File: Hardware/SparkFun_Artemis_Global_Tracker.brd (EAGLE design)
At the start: 50.8 x 63.5 mm, 209 parts, among them J1 IRIDIUM_9603N, J2 USB-C, J6 U.FL, J7 ANTENNA-GROUNDEDEDGE_SMA, J8 STANDOFFS_M2X0.4_STEEL_6MM, J9 STANDOFFS_M2X0.4_STEEL_6MM, Q1 5.8A/30V/35mΩ, Q2 20V/4.2A/52mΩ/1.4W, Q3 20V/4.2A/52mΩ/1.4W, Q4 600mA/40V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

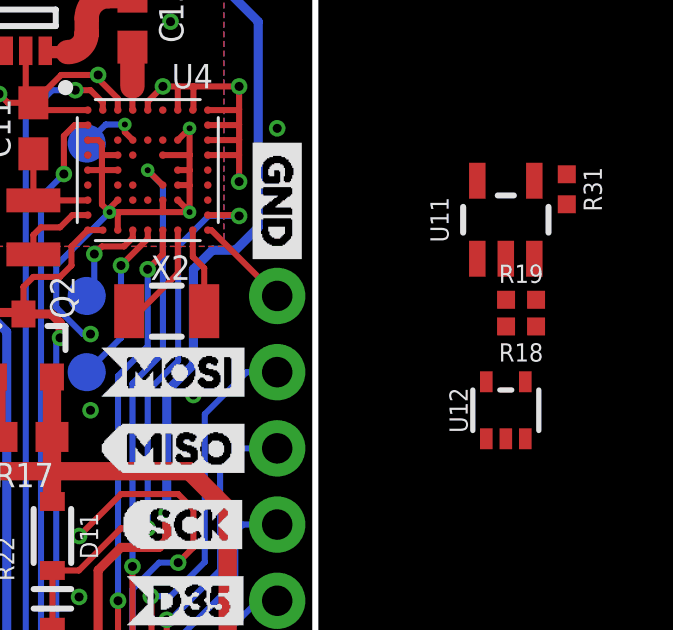
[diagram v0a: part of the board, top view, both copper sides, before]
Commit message: swapping names of U11 and U12 to avoid confusion
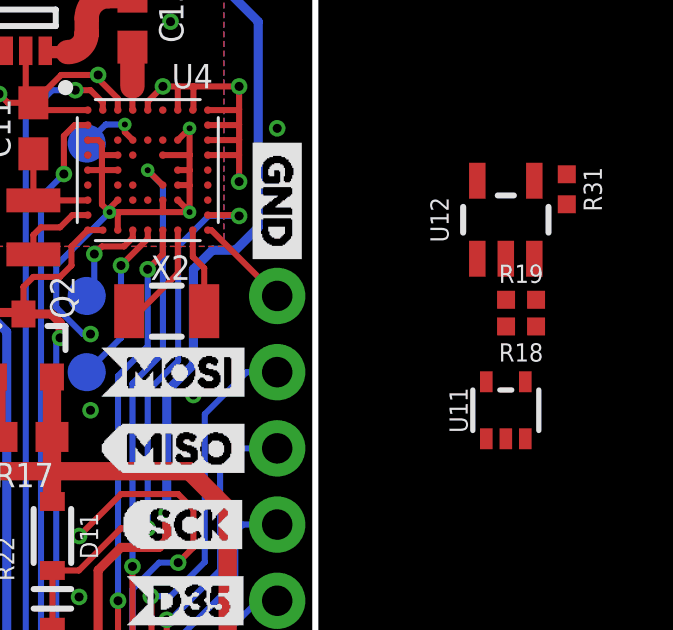
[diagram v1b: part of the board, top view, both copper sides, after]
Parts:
- U11: value 74LVC1G08SE -> 74LVC1G04SE; device SparkFun-IC-Logic:SOT23-5 -> SparkFun-IC-Logic:SOT353
- U12: value 74LVC1G04SE -> 74LVC1G08SE; device SparkFun-IC-Logic:SOT353 -> SparkFun-IC-Logic:SOT23-5
- moved U11 6.35 mm to (57.1, 41.9)
- moved U12 6.35 mm to (57.1, 48.3)
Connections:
- net 3.3V: now also U12.5; no longer U11.5
- net 3V3SW: now also U12.1; no longer U11.1
- net EXT_PWR: now also U11.2; no longer U12.2
- net LTC3225_VOUT: now also U11.5; no longer U12.5
- net N$31: now also U12.4; no longer U11.4
- net N$33: now also U12.2; no longer U11.2
- net N$7: now also U11.4; no longer U12.4
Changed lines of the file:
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@@
 <drawing>
 <settings>
-<setting alwaysvectorfont="yes"/>
+<setting alwaysvectorfont="no"/>
 <setting keepoldvectorfont="yes"/>
 <setting verticaltext="up"/>
@@
 <layer number="47" name="Measures" color="7" fill="1" visible="no" active="yes"/>
 <layer number="48" name="Document" color="7" fill="1" visible="no" active="yes"/>
-<layer number="49" name="Reference" color="7" fill="1" visible="yes" active="yes"/>
+<layer number="49" name="Reference" color="7" fill="1" visible="no" active="yes"/>
 <layer number="50" name="dxf" color="7" fill="1" visible="no" active="yes"/>
 <layer number="51" name="tDocu" color="6" fill="1" visible="yes" active="yes"/>
@@
 <attribute name="VALUE" x="57.658" y="45.031" size="0.6096" layer="27" font="vector" ratio="20" align="top-center"/>
 </element>
-<element name="U11" library="SparkFun-IC-Logic" package="SOT23-5" value="74LVC1G08SE" x="57.15" y="48.26" smashed="yes">
+<element name="U12" library="SparkFun-IC-Logic" package="SOT23-5" value="74LVC1G08SE" x="57.15" y="48.26" smashed="yes">
 <attribute name="NAME" x="55.245" y="48.26" size="0.6096" layer="25" font="vector" ratio="20" rot="R90" align="bottom-center"/>
 <attribute name="PROD_ID" value="IC-10841" x="57.15" y="48.26" size="1.778" layer="27" font="vector" ratio="15" display="off"/>
 <attribute name="VALUE" x="59.69" y="48.26" size="0.6096" layer="27" font="vector" ratio="20" rot="R90" align="bottom-center"/>
 </element>
-<element name="U12" library="SparkFun-IC-Logic" package="SOT353" value="74LVC1G04SE" x="57.15" y="41.91" smashed="yes">
+<element name="U11" library="SparkFun-IC-Logic" package="SOT353" value="74LVC1G04SE" x="57.15" y="41.91" smashed="yes">
 <attribute name="NAME" x="55.88" y="41.91" size="0.6096" layer="25" font="vector" ratio="20" rot="R90" align="bottom-center"/>
 <attribute name="PROD_ID" value="IC-10843" x="57.15" y="41.91" size="1.778" layer="27" font="vector" ratio="15" display="off"/>
@@
 <wire x1="13.97" y1="32.342" x2="13.97" y2="29.591" width="0.6096" layer="1"/>
 <wire x1="13.97" y1="29.591" x2="12.192" y2="27.813" width="0.6096" layer="1"/>
-<contactref element="U11" pad="5"/>
+<contactref element="U12" pad="5"/>
 <wire x1="42.0218" y1="43.0182" x2="56.2" y2="49.5601" width="0" layer="19" extent="1-1"/>
 </signal>
@@
 <wire x1="22.3032" y1="48.3088" x2="22.352" y2="48.26" width="0.2032" layer="1"/>
 <contactref element="R19" pad="2"/>
-<contactref element="U11" pad="3"/>
 <contactref element="U12" pad="3"/>
+<contactref element="U11" pad="3"/>
 <contactref element="R31" pad="2"/>
 <wire x1="58.1" y1="46.9599" x2="58.158" y2="45.593" width="0" layer="19" extent="1-1"/>
@@
 <wire x1="28.4132" y1="48.326" x2="28.4032" y2="48.316" width="0.6096" layer="1"/>
 <wire x1="28.4032" y1="48.316" x2="27.178" y2="48.316" width="0.6096" layer="1"/>
-<contactref element="U12" pad="2"/>
+<contactref element="U11" pad="2"/>
 <wire x1="45.847" y1="38.481" x2="57.15" y2="40.96" width="0" layer="19" extent="1-1"/>
 </signal>
@@
 <wire x1="10.922" y1="57.277" x2="10.922" y2="58.8146" width="0.4064" layer="1"/>
 <wire x1="10.922" y1="58.8146" x2="10.8458" y2="58.8908" width="0.3048" layer="1"/>
-<contactref element="U12" pad="5"/>
+<contactref element="U11" pad="5"/>
 <wire x1="34.193" y1="47.432" x2="56.5" y2="42.86" width="0" layer="19" extent="1-1"/>
 </signal>
@@
 <wire x1="41.0718" y1="45.1182" x2="41.021" y2="45.169" width="0.3048" layer="1"/>
 <wire x1="41.021" y1="45.169" x2="39.624" y2="45.169" width="0.3048" layer="1"/>
-<contactref element="U11" pad="1"/>
+<contactref element="U12" pad="1"/>
 <wire x1="43.716" y1="47.915" x2="56.2" y2="46.9599" width="0" layer="19" extent="1-1"/>
 </signal>
@@
 <signal name="N$31">
 <contactref element="U5" pad="6"/>
-<contactref element="U11" pad="4"/>
+<contactref element="U12" pad="4"/>
 <contactref element="R31" pad="1"/>
 <wire x1="59.182" y1="49.776" x2="58.1" y2="49.5601" width="0" layer="19" extent="1-1"/>
@@
 <contactref element="R18" pad="2"/>
 <contactref element="R19" pad="1"/>
-<contactref element="U11" pad="2"/>
+<contactref element="U12" pad="2"/>
 <wire x1="57.158" y1="45.593" x2="57.158" y2="44.704" width="0" layer="19" extent="1-1"/>
 <wire x1="57.15" y1="46.9599" x2="57.158" y2="45.593" width="0" layer="19" extent="1-1"/>
@@
 <signal name="N$7">
 <contactref element="R18" pad="1"/>
-<contactref element="U12" pad="4"/>
+<contactref element="U11" pad="4"/>
 <wire x1="57.8" y1="42.86" x2="58.158" y2="44.704" width="0" layer="19" extent="1-1"/>
 </signal>

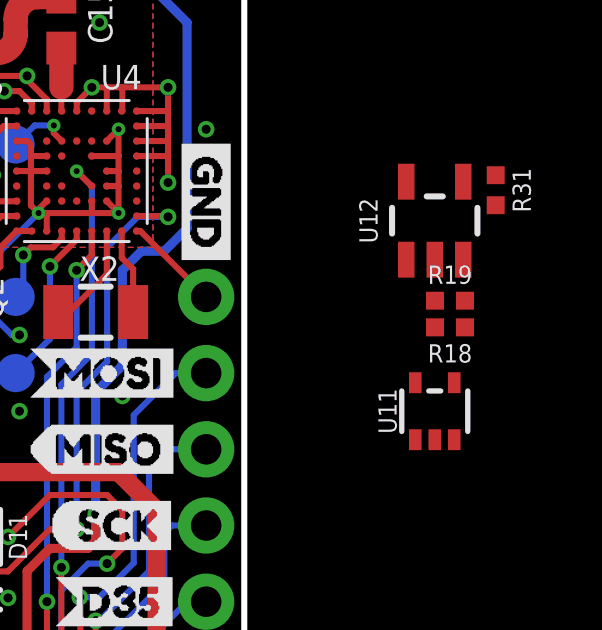
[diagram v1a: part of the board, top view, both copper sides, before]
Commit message: removed voltage divider (logic shift) from inverter to AND gate.
The AND gate is 5.5V tolerant, so we don't need to shift logic level
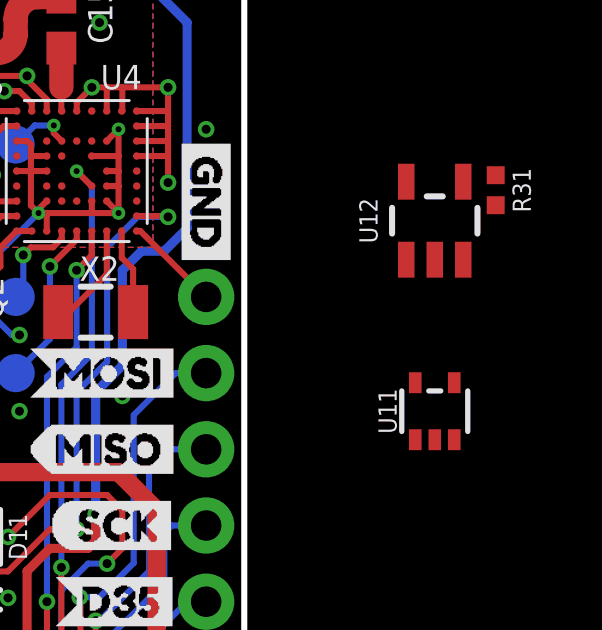
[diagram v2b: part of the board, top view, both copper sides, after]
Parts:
- removed R18: 20k, SparkFun-Resistors:0402-TIGHT
- removed R19: 33k, SparkFun-Resistors:0402-TIGHT
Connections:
- removed net N$7: R18.1, U11.4
- net GND: no longer R19.2
- net N$33: now also U11.4; no longer R18.2, R19.1

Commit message: powering U11 from 3.3V
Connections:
- net 3.3V: now also U11.5
- net LTC3225_VOUT: no longer U11.5
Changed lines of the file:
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@@
 <wire x1="13.97" y1="29.591" x2="12.192" y2="27.813" width="0.6096" layer="1"/>
 <contactref element="U12" pad="5"/>
-<wire x1="42.0218" y1="43.0182" x2="56.2" y2="49.5601" width="0" layer="19" extent="1-1"/>
+<contactref element="U11" pad="5"/>
+<wire x1="56.5" y1="42.86" x2="56.2" y2="49.5601" width="0" layer="19" extent="1-1"/>
+<wire x1="49.53" y1="30.48" x2="56.5" y2="42.86" width="0" layer="19" extent="1-1"/>
 </signal>
 <signal name="GND">
@@
 <wire x1="10.922" y1="57.277" x2="10.922" y2="58.8146" width="0.4064" layer="1"/>
 <wire x1="10.922" y1="58.8146" x2="10.8458" y2="58.8908" width="0.3048" layer="1"/>
-<contactref element="U11" pad="5"/>
-<wire x1="34.193" y1="47.432" x2="56.5" y2="42.86" width="0" layer="19" extent="1-1"/>
 </signal>
 <signal name="N$11">

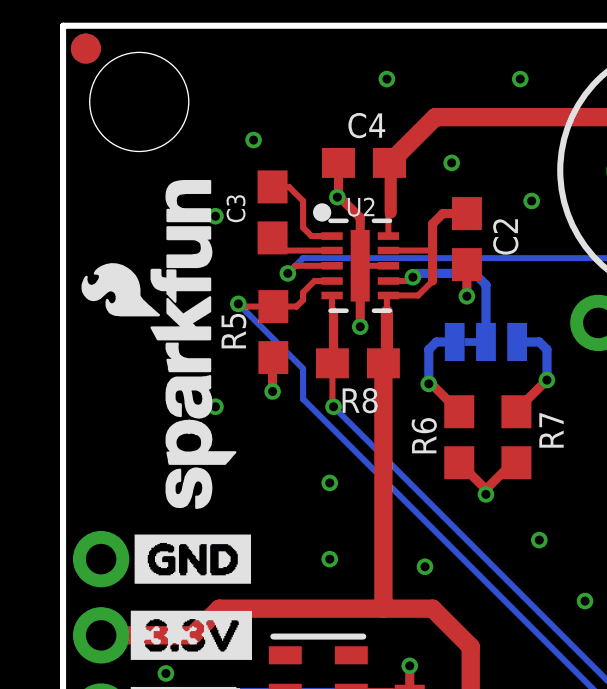
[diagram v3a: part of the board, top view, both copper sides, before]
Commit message: schematic tightening and moving most to first sheet
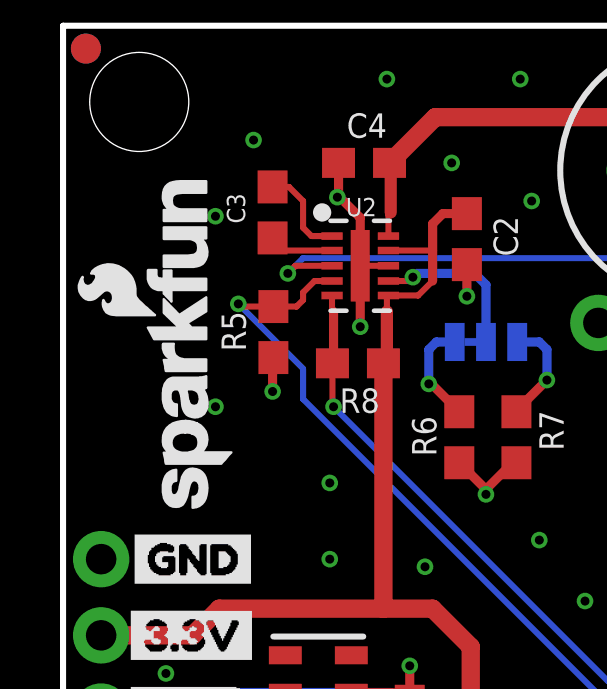
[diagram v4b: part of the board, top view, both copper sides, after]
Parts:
- removed FRAME4: FRAME-LETTER, SparkFun-Aesthetics:CREATIVE_COMMONS
- removed U$28: (no value), SparkFun-Aesthetics:SFE_LOGO_NAME_.1
- removed U$8: (no value), SparkFun-Aesthetics:SFE_LOGO_NAME_FLAME_.1
- added LOGO1: SFE_LOGO_NAME.1_INCH, SparkFun-Aesthetics:SFE_LOGO_NAME_.1
- added LOGO2: SFE_LOGO_NAME_FLAME.1_INCH, SparkFun-Aesthetics:SFE_LOGO_NAME_FLAME_.1

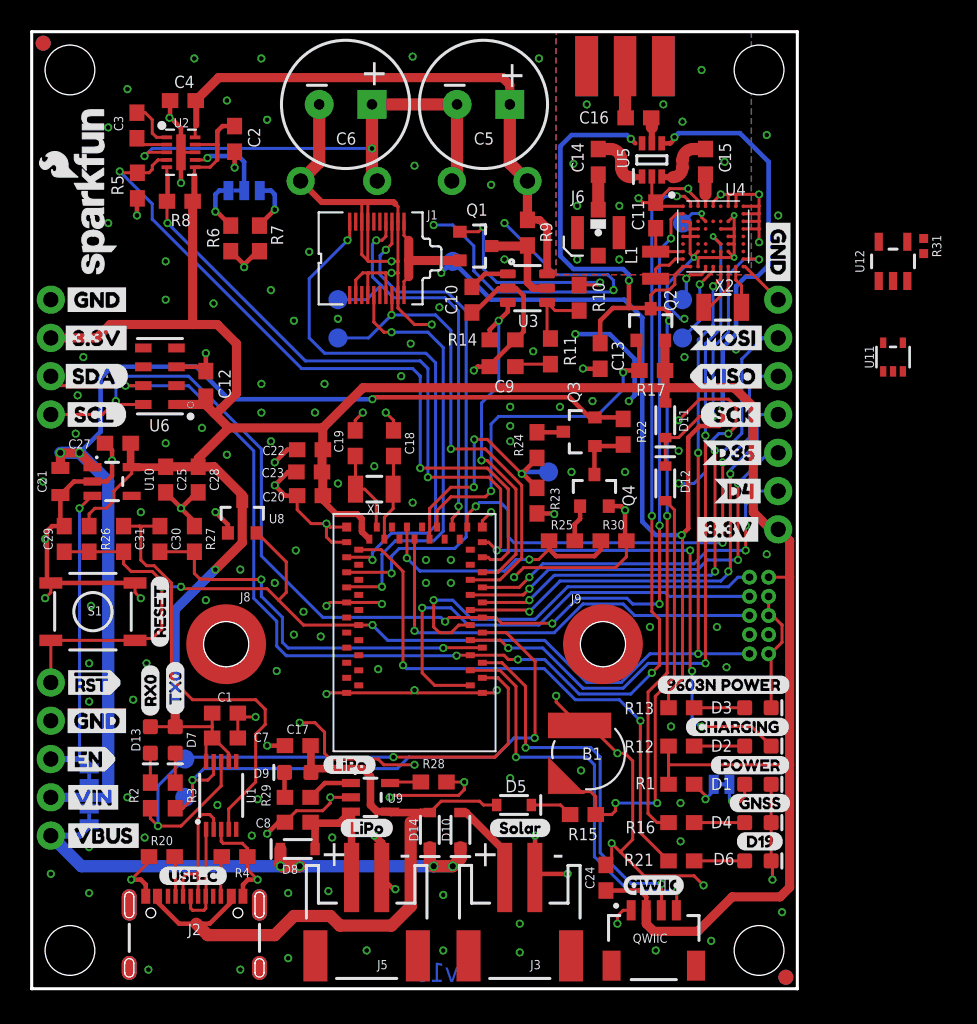
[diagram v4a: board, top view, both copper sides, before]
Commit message: antenna switch circuit added in
-added antenna switch protection circuit.
-a few parts moved to 0402 packages to make room
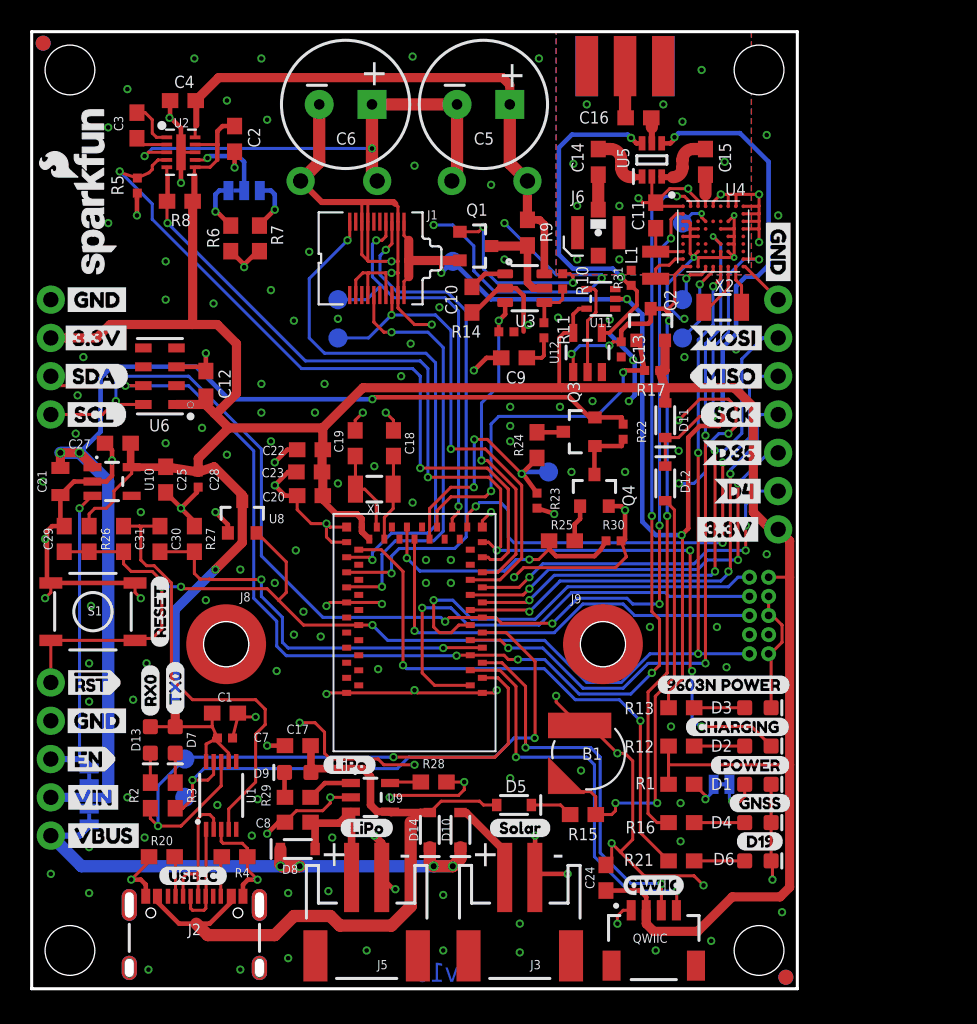
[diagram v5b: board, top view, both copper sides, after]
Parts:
- C13, C28, C7: device SparkFun-Capacitors:0603 -> SparkFun-Capacitors:0402-TIGHT
- FRAME3: value FRAME-LETTER -> FRAME-LETTERNO_PACKAGE; device SparkFun-Aesthetics:CREATIVE_COMMONS -> SparkFun-Aesthetics:DUMMY
- J2: device SparkFun-Connectors:USB-C-16P -> SparkFun-Connectors:USB-C-16P-2LAYER-PADS
- R10, R11: device SparkFun-Resistors:0603 -> SparkFun-Resistors:0402-TIGHT
- R14, R17, R22, R23, R30, R5: value 10k -> 10K; device SparkFun-Resistors:0603 -> SparkFun-Resistors:0402-TIGHT
- moved U12 21.2 mm to (36.9, 42.2)
- moved U11 19.8 mm to (37.8, 45.8), turned to 90 degrees
- moved R31 19.5 mm to (39.8, 47.2), turned to 90 degrees
- moved FRAME5 8.89 mm to (-7.62, -14.0)
- moved R10 1.54 mm to (35.2, 46.9)
- moved R11 1.46 mm to (34.0, 43.7)
- moved C13 1.46 mm to (39.1, 42.4)
- moved C9 0.96 mm to (32.0, 41.9)
- moved R14 0.59 mm to (31.5, 43.6)
- moved U3 0.18 mm to (32.7, 46.5)
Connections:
- net ARTEMIS_D13: now also VIN/3.1; no longer VIN/3.P$1
- net ARTEMIS_D24: now also TX1.1; no longer TX1.P$1
- net ARTEMIS_D25: now also RX1.1; no longer RX1.P$1
- net ARTEMIS_RX0: now also RX0.1; no longer RX0.P$1
- net ARTEMIS_TX0: now also TX0.1; no longer TX0.P$1
- net EXT_PWR: now also 5V3.1; no longer 5V3.P$1
- net N$25: now also SAFEBOOT.1; no longer SAFEBOOT.P$1
- net N$26: now also GPS_RX.1; no longer GPS_RX.P$1
- net N$27: now also GPS_TX.1; no longer GPS_TX.P$1
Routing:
- net N$31: track 0.00 -> 23.4 mm, vias 0 -> 2
- net 3V3SW: track 66.7 -> 49.3 mm
- net 3.3V: track 196.3 -> 204.4 mm
- net GND: track 313.7 -> 307.2 mm, vias 178 -> 179
- net N$33: track 0.00 -> 6.29 mm
- net N$12: track 14.1 -> 12.0 mm
- net N$13: track 4.83 -> 3.35 mm
- net EXT_PWR: track 89.5 -> 90.4 mm, vias 4 -> 5
- net ARTEMIS_D22: track 22.8 -> 22.0 mm
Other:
- board text added: "Paul Clark"
- board text added: "Revised by: Pete Lewis"

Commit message: Switched D8 to a P-CH MOSFET
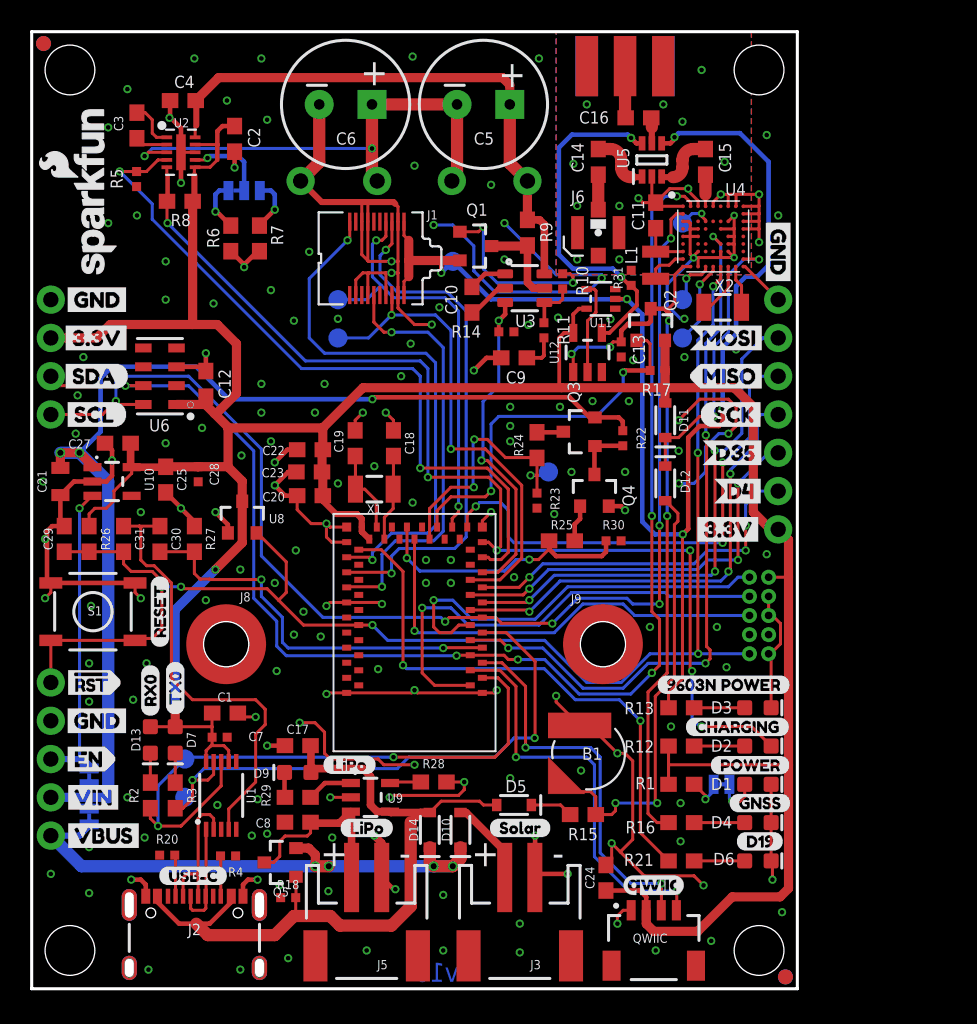
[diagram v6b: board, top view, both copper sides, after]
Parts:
- removed D8: 0.5A/40V/420mV, SparkFun-DiscreteSemi:SOD-323
- added Q5: 20V/4.2A/52mΩ/1.4W, SparkFun-DiscreteSemi:SOT23-3
- added R18: 10K, SparkFun-Resistors:0402-TIGHT
- R20, R4: device SparkFun-Resistors:0603 -> SparkFun-Resistors:0402-TIGHT
- moved R4 0.43 mm to (13.0, 8.81)
- moved R5 0.43 mm to (6.96, 53.7)
- moved R22 0.43 mm to (39.2, 36.5)
- moved R20 0.37 mm to (8.99, 8.86)
- moved C7 0.36 mm to (12.5, 16.7)
- moved C28 0.36 mm to (11.0, 34.1)
- moved R17 0.36 mm to (41.5, 41.0)
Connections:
- net GND: now also R18.1
- net VBUS: now also Q5.2; no longer D8.C
- net V_BATT: now also Q5.3; no longer D8.A
- net V_USB: now also Q5.1, R18.2
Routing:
- net GND: track 307.2 -> 268.1 mm
- net V_BATT: track 9.31 -> 12.6 mm
- net V_USB: track 46.8 -> 49.5 mm
- net 3.3V: track 204.4 -> 202.5 mm
- net VBUS: track 38.0 -> 36.8 mm
- net ARTEMIS_D26: track 24.1 -> 25.1 mm

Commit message: schematic cleanup/tightening
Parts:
- QWIIC: value QWIIC_RIGHT_ANGLE -> QWIIC_RA
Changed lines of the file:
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@@
 <attribute name="NAME" x="46.3296" y="26.3398" size="0.6096" layer="26" font="vector" ratio="20" rot="MR270"/>
 </element>
-<element name="QWIIC" library="SparkFun-Connectors" package="JST04_1MM_RA" value="QWIIC_RIGHT_ANGLE" x="41.275" y="5.207" smashed="yes">
+<element name="QWIIC" library="SparkFun-Connectors" package="JST04_1MM_RA" value="QWIIC_RA" x="41.275" y="5.207" smashed="yes">
 <attribute name="NAME" x="39.878" y="3.048" size="0.6096" layer="25" font="vector" ratio="20"/>
 <attribute name="PROD_ID" value="CONN-13694" x="41.275" y="5.207" size="1.778" layer="27" display="off"/>
